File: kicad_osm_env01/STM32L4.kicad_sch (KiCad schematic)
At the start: 36 parts, among them J6 Conn_02x03_Odd_Even, U6 STM32L433VCTx, Y1 8MHZ, Y2 Crystal

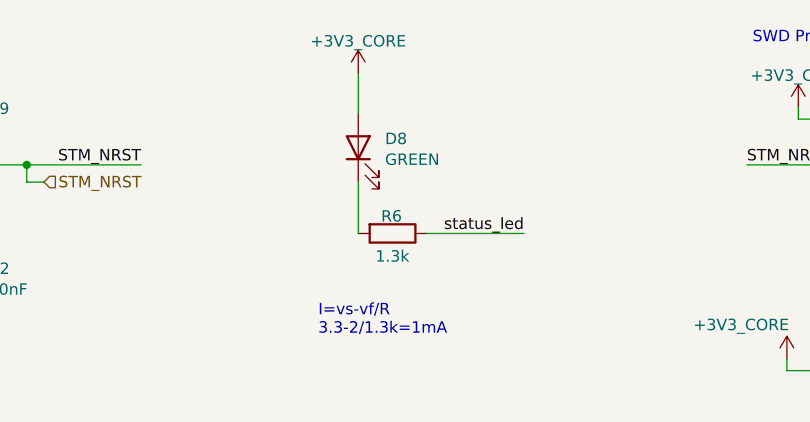
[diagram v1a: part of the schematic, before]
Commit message: removed battery circuit and add usb c to schematics
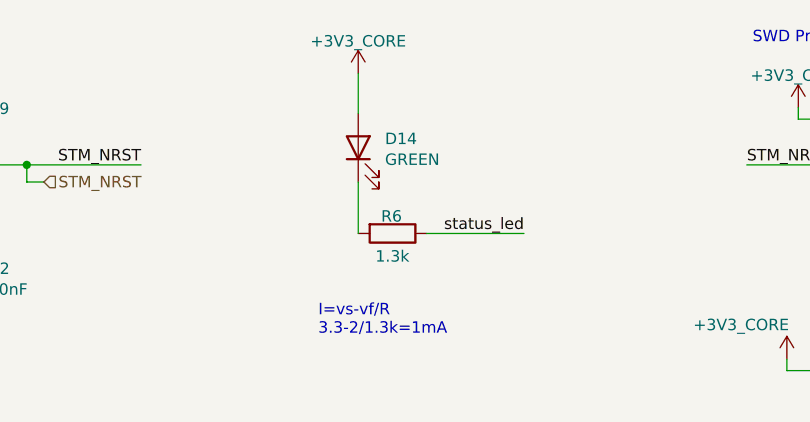
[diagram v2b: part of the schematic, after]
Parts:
- renumbered D8 to D14
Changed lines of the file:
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@@
   (symbol (lib_id "Device:LED") (at 228.6 31.115 90) (unit 1)
     (in_bom yes) (on_board yes) (dnp no)
-    (property "Reference" "D8" (at 231.5718 30.1244 90)
+    (property "Reference" "D14" (at 231.5718 30.1244 90)
       (effects (font (size 1.27 1.27)) (justify right))
     )
@@
       (project "OSM_env01"
         (path "/ab8b0540-9c9f-4195-88f5-7bed0b0a8ed6/00000000-0000-0000-0000-000060917dd5"
-          (reference "D8") (unit 1)
+          (reference "D14") (unit 1)
         )
       )

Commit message: removed io module and 5V regulator
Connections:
- net status_led: now also U6.85 (PD4/DFSDM_CKIN0/FMC_NOE/SPI2_MOSI/USART2_DE/USART2_RTS); no longer U6.23 (ADC1_IN5/ADC2_IN5/OPAMP1_VINP/RTC_TAMP2/SAI1_EXTCLK/SYS_WKUP1/TIM2_CH1/TIM2_ETR/TIM5_CH1/TIM8_ETR/UART4_TX/USART2_CTS/PA0)
- net GPIO18: now reaches U6.81 (PD0/CAN1_RX/DFSDM_DATIN7/FMC_D2/FMC_DA2/SPI2_NSS)
- net GPIO19: now reaches U6.82 (PD1/CAN1_TX/DFSDM_CKIN7/FMC_D3/FMC_DA3/SPI2_SCK)
- net GPIO5: now reaches U6.84 (PD3/DFSDM_DATIN0/FMC_CLK/SPI2_MISO/USART2_CTS)
- net GPIO20: now reaches U6.86 (PD5/FMC_NWE/USART2_TX)
- net +3V3_CORE renamed +3V3
- new net ADC9: U6.23 (ADC1_IN5/ADC2_IN5/OPAMP1_VINP/RTC_TAMP2/SAI1_EXTCLK/SYS_WKUP1/TIM2_CH1/TIM2_ETR/TIM5_CH1/TIM8_ETR/UART4_TX/USART2_CTS/PA0)
- no-connect marks 32 -> 27

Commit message: updated schematics with 5V ored circuit and new 3v3 regulator
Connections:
- net ADC6 is gone; now on net ADC4: U6.36 (ADC1_IN16/ADC2_IN16/COMP1_INM/DFSDM_DATIN0/LCD_SEG6/LPTIM2_IN1/QUADSPI_BK1_IO0/TIM1_CH3N/TIM3_CH4/TIM8_CH3N/USART3_DE/USART3_RTS/PB1)
- net ADC8 is gone; now on net ADC5: U6.29 (ADC1_IN9/ADC2_IN9/DAC1_OUT1/LPTIM2_OUT/SAI1_FS_B/SPI1_NSS/SPI3_NSS/USART2_CK/PA4)
- net ADC9 is gone; now on net status_led: U6.23 (ADC1_IN5/ADC2_IN5/OPAMP1_VINP/RTC_TAMP2/SAI1_EXTCLK/SYS_WKUP1/TIM2_CH1/TIM2_ETR/TIM5_CH1/TIM8_ETR/UART4_TX/USART2_CTS/PA0)
- net GPIO13 is gone; now on net GPIO9: U6.54 (ADC1_EXTI15/ADC2_EXTI15/ADC3_EXTI15/DFSDM_CKIN2/LCD_SEG15/RTC_REFIN/SAI2_SD_A/SPI2_MOSI/SWPMI1_SUSPEND/TIM15_CH2/TIM1_CH3N/TIM8_CH3N/TSC_G1_IO4/PB15)
- net GPIO15 is gone; now on net GPIO10: U6.52 (DFSDM_CKIN1/I2C2_SCL/LCD_SEG13/LPUART1_CTS/SAI2_SCK_A/SPI2_SCK/SWPMI1_TX/TIM15_CH1N/TIM1_CH1N/TSC_G1_IO2/USART3_CTS/PB13)
- net GPIO16 is gone; now on net GPIO11: U6.79 (ADC1_EXTI11/ADC2_EXTI11/ADC3_EXTI11/LCD_COM5/LCD_SEG29/LCD_SEG41/SAI2_MCLK_B/SDMMC1_D3/SPI3_MISO/TSC_G3_IO3/UART4_RX/USART3_RX/PC11)
- net GPIO17 is gone; now on net GPIO12: U6.51 (DFSDM_DATIN1/I2C2_SMBA/LCD_SEG12/LPUART1_DE/LPUART1_RTS/SAI2_FS_A/SPI2_NSS/SWPMI1_IO/TIM15_BKIN/TIM1_BKIN/TIM1_BKIN_COMP2/TSC_G1_IO1/USART3_CK/PB12)
- net ADC1: now also U6.24 (ADC1_IN6/ADC2_IN6/LCD_SEG0/OPAMP1_VINM/TIM15_CH1N/TIM2_CH2/TIM5_CH2/UART4_RX/USART2_DE/USART2_RTS/PA1); no longer U6.16 (ADC1_IN2/ADC2_IN2/ADC3_IN2/DFSDM_CKIN4/I2C3_SDA/LCD_SEG19/LPTIM1_OUT/LPUART1_TX/PC1)
- net ADC2: now also U6.18 (ADC1_IN4/ADC2_IN4/ADC3_IN4/LCD_VLCD/LPTIM1_ETR/LPTIM2_ETR/SAI1_SD_A/SPI2_MOSI/PC3); no longer U6.24 (ADC1_IN6/ADC2_IN6/LCD_SEG0/OPAMP1_VINM/TIM15_CH1N/TIM2_CH2/TIM5_CH2/UART4_RX/USART2_DE/USART2_RTS/PA1)
- net ADC3: now also U6.35 (ADC1_IN15/ADC2_IN15/COMP1_OUT/LCD_SEG5/OPAMP2_VOUT/QUADSPI_BK1_IO1/TIM1_CH2N/TIM3_CH3/TIM8_CH2N/USART3_CK/PB0); no longer U6.17 (ADC1_IN3/ADC2_IN3/ADC3_IN3/DFSDM_CKOUT/LCD_SEG20/LPTIM1_IN2/SPI2_MISO/PC2)
- net ADC4: no longer U6.18 (ADC1_IN4/ADC2_IN4/ADC3_IN4/LCD_VLCD/LPTIM1_ETR/LPTIM2_ETR/SAI1_SD_A/SPI2_MOSI/PC3)
- net ADC5: no longer U6.35 (ADC1_IN15/ADC2_IN15/COMP1_OUT/LCD_SEG5/OPAMP2_VOUT/QUADSPI_BK1_IO1/TIM1_CH2N/TIM3_CH3/TIM8_CH2N/USART3_CK/PB0)
- net GPIO10: no longer U6.77 (ADC1_EXTI15/ADC2_EXTI15/ADC3_EXTI15/LCD_SEG17/SAI2_FS_B/SPI1_NSS/SPI3_NSS/SYS_JTDI/TIM2_CH1/TIM2_ETR/TSC_G3_IO1/UART4_DE/UART4_RTS/PA15)
- net GPIO11: no longer U6.64 (DFSDM_DATIN3/LCD_SEG25/SAI2_MCLK_B/SDMMC1_D7/TIM3_CH2/TIM8_CH2/TSC_G4_IO2/PC7)
- net GPIO12: no longer U6.53 (DFSDM_DATIN2/I2C2_SDA/LCD_SEG14/SAI2_MCLK_A/SPI2_MISO/SWPMI1_RX/TIM15_CH1/TIM1_CH2N/TIM8_CH2N/TSC_G1_IO3/USART3_DE/USART3_RTS/PB14)
- net GPIO4: now also U6.89 (COMP2_INM/LCD_SEG7/SAI1_SCK_B/SPI1_SCK/SPI3_SCK/SYS_JTDO-SWO/TIM2_CH2/USART1_DE/USART1_RTS/PB3); no longer U6.66 (DAC1_EXTI9/LCD_SEG27/SAI2_EXTCLK/SDMMC1_D1/TIM3_CH4/TIM8_BKIN2/TIM8_BKIN2_COMP1/TIM8_CH4/TSC_G4_IO4/USB_OTG_FS_NOE/PC9)
- net GPIO5: now also U6.91 (COMP2_OUT/I2C1_SMBA/LCD_SEG9/LPTIM1_IN1/SAI1_SD_B/SPI1_MOSI/SPI3_MOSI/TIM16_BKIN/TIM3_CH2/TSC_G2_IO2/UART5_CTS/USART1_CK/PB5); no longer U6.84 (PD3/DFSDM_DATIN0/FMC_CLK/SPI2_MISO/USART2_CTS)
- net GPIO6: now also U6.77 (ADC1_EXTI15/ADC2_EXTI15/ADC3_EXTI15/LCD_SEG17/SAI2_FS_B/SPI1_NSS/SPI3_NSS/SYS_JTDI/TIM2_CH1/TIM2_ETR/TSC_G3_IO1/UART4_DE/UART4_RTS/PA15); no longer U6.89 (COMP2_INM/LCD_SEG7/SAI1_SCK_B/SPI1_SCK/SPI3_SCK/SYS_JTDO-SWO/TIM2_CH2/USART1_DE/USART1_RTS/PB3)
- net GPIO7: now also U6.64 (DFSDM_DATIN3/LCD_SEG25/SAI2_MCLK_B/SDMMC1_D7/TIM3_CH2/TIM8_CH2/TSC_G4_IO2/PC7); no longer U6.80 (LCD_COM6/LCD_SEG30/LCD_SEG42/SAI2_SD_B/SDMMC1_CK/SPI3_MOSI/TSC_G3_IO4/UART5_TX/USART3_CK/PC12)
- net GPIO8: now also U6.53 (DFSDM_DATIN2/I2C2_SDA/LCD_SEG14/SAI2_MCLK_A/SPI2_MISO/SWPMI1_RX/TIM15_CH1/TIM1_CH2N/TIM8_CH2N/TSC_G1_IO3/USART3_DE/USART3_RTS/PB14); no longer U6.90 (COMP2_INP/LCD_SEG8/SAI1_MCLK_B/SPI1_MISO/SPI3_MISO/SYS_JTRST/TIM17_BKIN/TIM3_CH1/TSC_G2_IO1/UART5_DE/UART5_RTS/USART1_CTS/PB4)
- net GPIO9: no longer U6.91 (COMP2_OUT/I2C1_SMBA/LCD_SEG9/LPTIM1_IN1/SAI1_SD_B/SPI1_MOSI/SPI3_MOSI/TIM16_BKIN/TIM3_CH2/TSC_G2_IO2/UART5_CTS/USART1_CK/PB5)
- net status_led: no longer U6.85 (PD4/DFSDM_CKIN0/FMC_NOE/SPI2_MOSI/USART2_DE/USART2_RTS)
- net ADC7: no longer names the net of U6.15 (ADC1_IN1/ADC2_IN1/ADC3_IN1/DFSDM_DATIN4/I2C3_SCL/LCD_SEG18/LPTIM1_IN1/LPTIM2_IN1/LPUART1_RX/PC0)
- net GPIO14: no longer names the net of U6.83 (PD2/LCD_COM7/LCD_SEG31/LCD_SEG43/SDMMC1_CMD/TIM3_ETR/TSC_SYNC/UART5_RX/USART3_DE/USART3_RTS)
- net GPIO18: no longer names the net of U6.81 (PD0/CAN1_RX/DFSDM_DATIN7/FMC_D2/FMC_DA2/SPI2_NSS)
- net GPIO19: no longer names the net of U6.82 (PD1/CAN1_TX/DFSDM_CKIN7/FMC_D3/FMC_DA3/SPI2_SCK)
- net GPIO20: no longer names the net of U6.86 (PD5/FMC_NWE/USART2_TX)
- no-connect marks 27 -> 39

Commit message: assigned all footprints
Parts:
- removed J6: Conn_02x03_Odd_Even, Connector_PinHeader_1.27mm:PinHeader_2x03_P1.27mm_Vertical, symbol Connector_Generic:Conn_02x03_Odd_Even
- removed R30: DNF, Resistor_SMD:R_0402_1005Metric, symbol Device:R
- removed S1: B3U-1100P, Button_Switch_SMD:SW_SPST_B3U-1100P, symbol Devtank:B3U-1100P
- added J10: Conn_01x05, Connector_PinHeader_2.54mm:PinHeader_1x05_P2.54mm_Vertical, symbol Connector_Generic:Conn_01x05
- added SW201: PTS810SJK250SMTR LFS, Button_Switch_SMD:SW_SPST_PTS810, symbol Switch:SW_Push
- C28, C29, C30, C43, C44, C51, C62, C64, C68: Voltage (none) -> 50V
- R119, R16: value 10k -> 10K
- R6: value 1.3k -> 1.3K; footprint Resistor_SMD:R_0603_1608Metric -> Resistor_SMD:R_0402_1005Metric
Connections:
- net +3V3: now also J10.1 (Pin_1)
- net GND: now also J10.2 (Pin_2), SW201.1
- net STM_NRST: now also J10.5 (Pin_5), SW201.2
- net SWCLK: now also J10.3 (Pin_3)
- net SWD_IO: now also J10.4 (Pin_4)
- no-connect marks 39 -> 38
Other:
- note added: "SWD Programming Header +3V3 and STM_NRST not to be used when 5V input is connected"
- note removed: "SWD Programming Header direct connect"
- moved on the sheet: R15, R16

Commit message: updated schematics
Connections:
- net GPIO12 is gone; now on net GPIO11: U6.51 (DFSDM_DATIN1/I2C2_SMBA/LCD_SEG12/LPUART1_DE/LPUART1_RTS/SAI2_FS_A/SPI2_NSS/SWPMI1_IO/TIM15_BKIN/TIM1_BKIN/TIM1_BKIN_COMP2/TSC_G1_IO1/USART3_CK/PB12)
- net GPIO10: now also U6.79 (ADC1_EXTI11/ADC2_EXTI11/ADC3_EXTI11/LCD_COM5/LCD_SEG29/LCD_SEG41/SAI2_MCLK_B/SDMMC1_D3/SPI3_MISO/TSC_G3_IO3/UART4_RX/USART3_RX/PC11); no longer U6.52 (DFSDM_CKIN1/I2C2_SCL/LCD_SEG13/LPUART1_CTS/SAI2_SCK_A/SPI2_SCK/SWPMI1_TX/TIM15_CH1N/TIM1_CH1N/TSC_G1_IO2/USART3_CTS/PB13)
- net GPIO11: no longer U6.79 (ADC1_EXTI11/ADC2_EXTI11/ADC3_EXTI11/LCD_COM5/LCD_SEG29/LCD_SEG41/SAI2_MCLK_B/SDMMC1_D3/SPI3_MISO/TSC_G3_IO3/UART4_RX/USART3_RX/PC11)
- net GPIO7: now also U6.53 (DFSDM_DATIN2/I2C2_SDA/LCD_SEG14/SAI2_MCLK_A/SPI2_MISO/SWPMI1_RX/TIM15_CH1/TIM1_CH2N/TIM8_CH2N/TSC_G1_IO3/USART3_DE/USART3_RTS/PB14)
- net GPIO8: now also U6.54 (ADC1_EXTI15/ADC2_EXTI15/ADC3_EXTI15/DFSDM_CKIN2/LCD_SEG15/RTC_REFIN/SAI2_SD_A/SPI2_MOSI/SWPMI1_SUSPEND/TIM15_CH2/TIM1_CH3N/TIM8_CH3N/TSC_G1_IO4/PB15); no longer U6.53 (DFSDM_DATIN2/I2C2_SDA/LCD_SEG14/SAI2_MCLK_A/SPI2_MISO/SWPMI1_RX/TIM15_CH1/TIM1_CH2N/TIM8_CH2N/TSC_G1_IO3/USART3_DE/USART3_RTS/PB14)
- net GPIO9: now also U6.52 (DFSDM_CKIN1/I2C2_SCL/LCD_SEG13/LPUART1_CTS/SAI2_SCK_A/SPI2_SCK/SWPMI1_TX/TIM15_CH1N/TIM1_CH1N/TSC_G1_IO2/USART3_CTS/PB13); no longer U6.54 (ADC1_EXTI15/ADC2_EXTI15/ADC3_EXTI15/DFSDM_CKIN2/LCD_SEG15/RTC_REFIN/SAI2_SD_A/SPI2_MOSI/SWPMI1_SUSPEND/TIM15_CH2/TIM1_CH3N/TIM8_CH3N/TSC_G1_IO4/PB15)
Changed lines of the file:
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@@
     (effects (font (size 1.27 1.27)) (justify left))
   )
-  (hierarchical_label "GPIO10" (shape input) (at 392.43 181.61 0) (fields_autoplaced)
+  (hierarchical_label "GPIO9" (shape input) (at 392.43 181.61 0) (fields_autoplaced)
     (effects (font (size 1.27 1.27)) (justify left))
   )
@@
     (effects (font (size 1.27 1.27)) (justify left))
   )
-  (hierarchical_label "GPIO8" (shape input) (at 392.43 184.15 0) (fields_autoplaced)
+  (hierarchical_label "GPIO7" (shape input) (at 392.43 184.15 0) (fields_autoplaced)
     (effects (font (size 1.27 1.27)) (justify left))
   )
@@
     (effects (font (size 1.27 1.27)) (justify left))
   )
-  (hierarchical_label "GPIO12" (shape input) (at 392.43 179.07 0) (fields_autoplaced)
+  (hierarchical_label "GPIO11" (shape input) (at 392.43 179.07 0) (fields_autoplaced)
     (effects (font (size 1.27 1.27)) (justify left))
   )
@@
     (effects (font (size 1.27 1.27)) (justify left))
   )
-  (hierarchical_label "GPIO11" (shape input) (at 393.7 219.71 0) (fields_autoplaced)
+  (hierarchical_label "GPIO10" (shape input) (at 393.7 219.71 0) (fields_autoplaced)
     (effects (font (size 1.27 1.27)) (justify left))
   )
@@
     (effects (font (size 1.27 1.27)) (justify left))
   )
-  (hierarchical_label "GPIO9" (shape input) (at 392.43 186.69 0) (fields_autoplaced)
+  (hierarchical_label "GPIO8" (shape input) (at 392.43 186.69 0) (fields_autoplaced)
     (effects (font (size 1.27 1.27)) (justify left))
   )

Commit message: updated stm32 pinmap
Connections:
- net GPIO4: now also U6.80 (LCD_COM6/LCD_SEG30/LCD_SEG42/SAI2_SD_B/SDMMC1_CK/SPI3_MOSI/TSC_G3_IO4/UART5_TX/USART3_CK/PC12); no longer U6.89 (COMP2_INM/LCD_SEG7/SAI1_SCK_B/SPI1_SCK/SPI3_SCK/SYS_JTDO-SWO/TIM2_CH2/USART1_DE/USART1_RTS/PB3)
- net GPIO7: no longer U6.64 (DFSDM_DATIN3/LCD_SEG25/SAI2_MCLK_B/SDMMC1_D7/TIM3_CH2/TIM8_CH2/TSC_G4_IO2/PC7)
- no-connect marks 38 -> 39
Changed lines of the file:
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@@
   (no_connect (at 380.365 158.75))
   (no_connect (at 380.365 191.77))
+  (no_connect (at 380.365 156.21))
   (no_connect (at 60.325 201.93))
   (no_connect (at 60.325 194.31))
   (no_connect (at 380.365 194.31))
   (no_connect (at 60.325 191.77))
-  (no_connect (at 380.365 222.25))
+  (no_connect (at 380.365 209.55))
   (wire (pts (xy 83.82 54.61) (xy 83.82 32.385))
     (stroke (width 0) (type default))
@@
     (stroke (width 0) (type default))
   )
-  (wire (pts (xy 380.365 209.55) (xy 392.43 209.55))
-    (stroke (width 0) (type default))
-  )
   (wire (pts (xy 74.93 40.64) (xy 62.865 40.64))
     (stroke (width 0) (type default))
@@
     (stroke (width 0) (type default))
   )
-  (wire (pts (xy 380.365 156.21) (xy 392.43 156.21))
+  (wire (pts (xy 380.365 222.25) (xy 392.43 222.25))
     (stroke (width 0) (type default))
   )
@@
     (effects (font (size 1.27 1.27)) (justify left))
   )
-  (hierarchical_label "GPIO4" (shape input) (at 392.43 156.21 0) (fields_autoplaced)
+  (hierarchical_label "GPIO4" (shape input) (at 392.43 222.25 0) (fields_autoplaced)
     (effects (font (size 1.27 1.27)) (justify left))
   )
@@
     (effects (font (size 1.27 1.27)) (justify left))
   )
-  (hierarchical_label "GPIO7" (shape input) (at 392.43 209.55 0) (fields_autoplaced)
-    (effects (font (size 1.27 1.27)) (justify left))
-  )

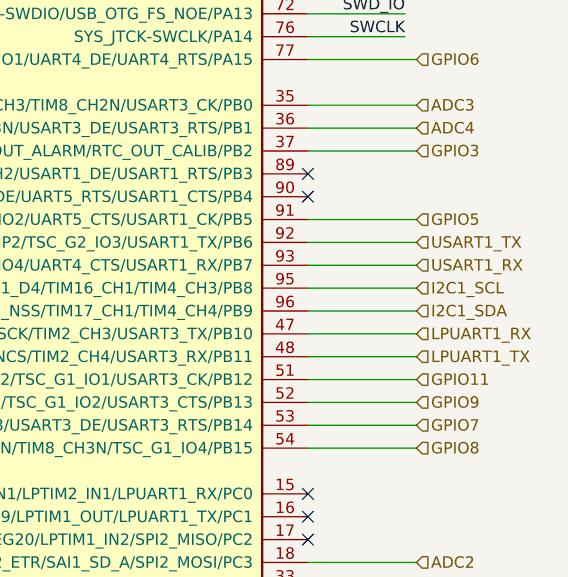
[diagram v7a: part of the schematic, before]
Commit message: layout updated with a few ic packages due to errors, silk screen tidy up, logos added, minor update to rs232 schematics and pinmap to stm
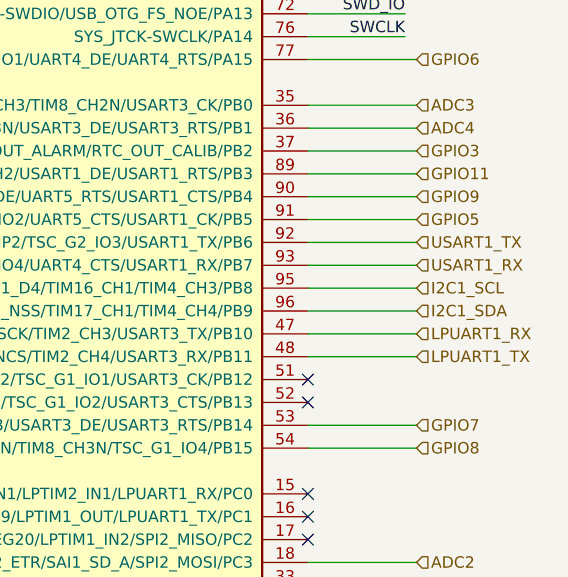
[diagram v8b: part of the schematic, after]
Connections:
- net GPIO11: now also U6.89 (COMP2_INM/LCD_SEG7/SAI1_SCK_B/SPI1_SCK/SPI3_SCK/SYS_JTDO-SWO/TIM2_CH2/USART1_DE/USART1_RTS/PB3); no longer U6.51 (DFSDM_DATIN1/I2C2_SMBA/LCD_SEG12/LPUART1_DE/LPUART1_RTS/SAI2_FS_A/SPI2_NSS/SWPMI1_IO/TIM15_BKIN/TIM1_BKIN/TIM1_BKIN_COMP2/TSC_G1_IO1/USART3_CK/PB12)
- net GPIO9: now also U6.90 (COMP2_INP/LCD_SEG8/SAI1_MCLK_B/SPI1_MISO/SPI3_MISO/SYS_JTRST/TIM17_BKIN/TIM3_CH1/TSC_G2_IO1/UART5_DE/UART5_RTS/USART1_CTS/PB4); no longer U6.52 (DFSDM_CKIN1/I2C2_SCL/LCD_SEG13/LPUART1_CTS/SAI2_SCK_A/SPI2_SCK/SWPMI1_TX/TIM15_CH1N/TIM1_CH1N/TSC_G1_IO2/USART3_CTS/PB13)
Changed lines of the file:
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@@
   (no_connect (at 60.325 153.67))
   (no_connect (at 380.365 196.85))
+  (no_connect (at 380.365 179.07))
   (no_connect (at 60.325 199.39))
   (no_connect (at 60.325 222.25))
@@
   (no_connect (at 60.325 209.55))
   (no_connect (at 60.325 207.01))
-  (no_connect (at 380.365 158.75))
+  (no_connect (at 380.365 181.61))
   (no_connect (at 380.365 191.77))
-  (no_connect (at 380.365 156.21))
   (no_connect (at 60.325 201.93))
   (no_connect (at 60.325 194.31))
@@
     (stroke (width 0) (type default))
   )
-  (wire (pts (xy 380.365 179.07) (xy 392.43 179.07))
+  (wire (pts (xy 380.365 156.21) (xy 392.43 156.21))
     (stroke (width 0) (type default))
   )
@@
     (stroke (width 0) (type default))
   )
-  (wire (pts (xy 392.43 181.61) (xy 380.365 181.61))
+  (wire (pts (xy 392.43 158.75) (xy 380.365 158.75))
     (stroke (width 0) (type default))
   )
@@
     (effects (font (size 1.27 1.27)) (justify left))
   )
-  (hierarchical_label "GPIO9" (shape input) (at 392.43 181.61 0) (fields_autoplaced)
+  (hierarchical_label "GPIO9" (shape input) (at 392.43 158.75 0) (fields_autoplaced)
     (effects (font (size 1.27 1.27)) (justify left))
   )
@@
     (effects (font (size 1.27 1.27)) (justify left))
   )
-  (hierarchical_label "GPIO11" (shape input) (at 392.43 179.07 0) (fields_autoplaced)
-    (effects (font (size 1.27 1.27)) (justify left))
-  )
+  (hierarchical_label "GPIO11" (shape input) (at 392.43 156.21 0) (fields_autoplaced)
+    (effects (font (size 1.27 1.27)) (justify left))
+  )
